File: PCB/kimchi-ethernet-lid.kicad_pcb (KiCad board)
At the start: 4 copper layers, 65 x 32 mm, 67 parts, among them J1 DF40HC(3.5)-60DS, J2 DF40HC(3.5)-60DS, J3 ARJM11C7-502-AB-ER2-T, U1 24C32, U2 TLV75712PDBVR, U3 KSZ9031RNXCC, Y1 ABM3-25.000MHZ-D2Y-T

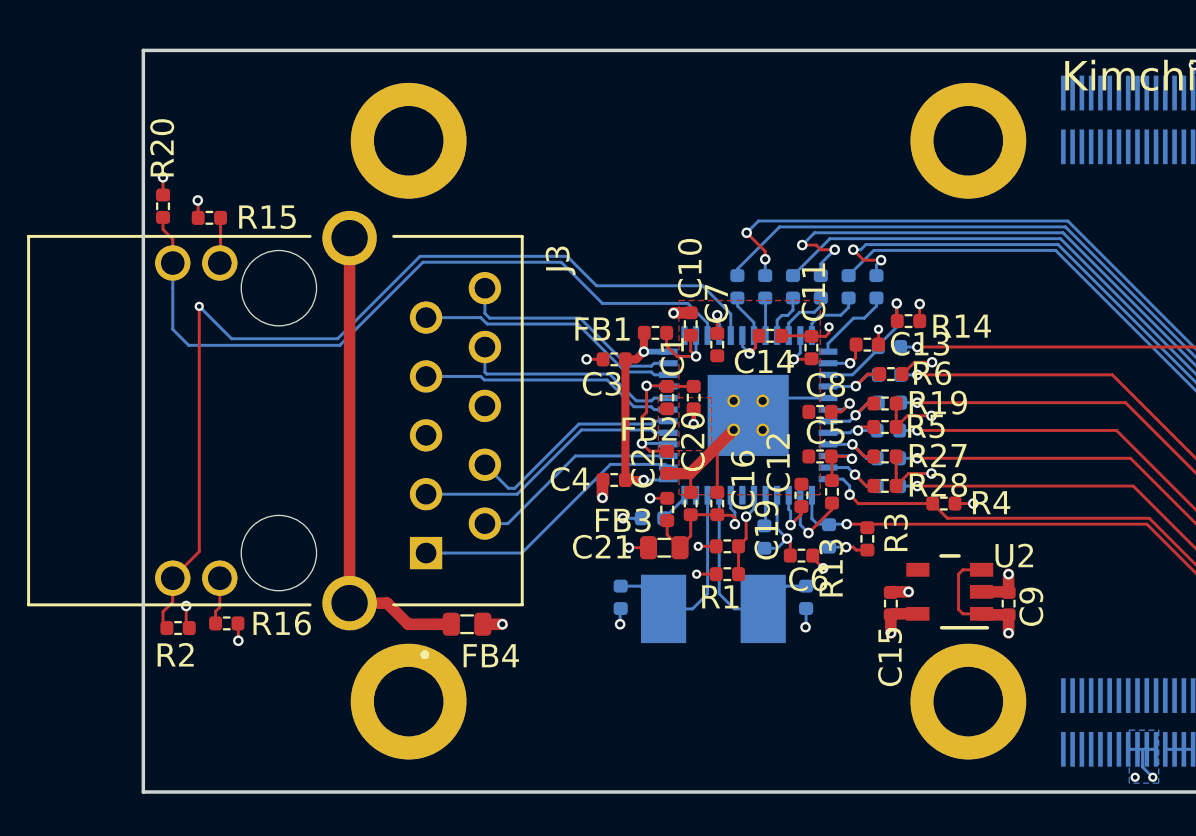
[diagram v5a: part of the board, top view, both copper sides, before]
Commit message: Silkscreen Tweak and BOM
Tweaked silkscreen text size and created order BOM
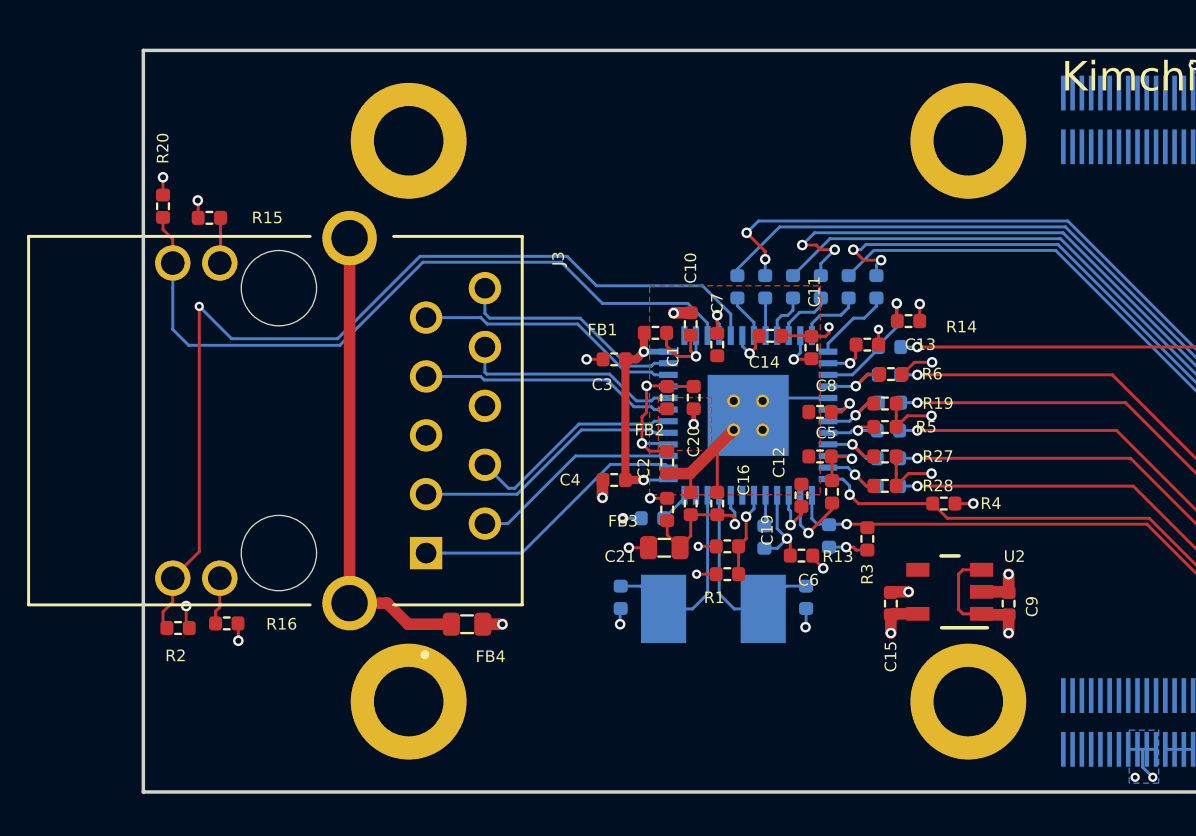
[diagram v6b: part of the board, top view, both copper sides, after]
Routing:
- net VDD_PHY_1V2: track 43.2 -> 44.1 mm

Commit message: DRC and Sys_Reset
Fixed some small DRC violations. zeroed out soldermask settings so that fab can decide their own. Tied SYS_RESET signal to muxable GPIO pin on Kimchi header.
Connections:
- J2 pad 31: SAI3_TXC -> /SYS_RESET
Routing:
- net /SYS_RESET: track 3.68 -> 32.1 mm, vias 1 -> 2
- net VDD_PHY_1V2: track 44.1 -> 45.2 mm
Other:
- rule pad_to_mask_clearance: 0.0508 -> 0
